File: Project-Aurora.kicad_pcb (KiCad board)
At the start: 4 copper layers, 285 x 94.6 mm, 266 parts, among them P1 USB_OTG, P2 FLASH_HDR, SW1 Reset, SW10 SW_PUSH, SW11 SW_PUSH, SW12 SW_PUSH, SW13 SW_PUSH, SW14 SW_PUSH, SW15 SW_PUSH, SW16 SW_PUSH, SW17 SW_PUSH, SW18 SW_PUSH, SW19 SW_PUSH, SW2 SW_PUSH, SW20 SW_PUSH, SW21 SW_PUSH, SW22 SW_PUSH, SW23 SW_PUSH, SW24 SW_PUSH, SW25 SW_PUSH, SW26 SW_PUSH, SW27 SW_PUSH, SW28 SW_PUSH, SW29 SW_PUSH, SW3 SW_PUSH, SW30 SW_PUSH, SW31 SW_PUSH, SW32 SW_PUSH, SW33 SW_PUSH, SW34 SW_PUSH, SW35 SW_PUSH, SW36 SW_PUSH, SW37 SW_PUSH, SW38 SW_PUSH, SW39 SW_PUSH, SW4 SW_PUSH, SW40 SW_PUSH, SW41 SW_PUSH, SW42 SW_PUSH, SW43 SW_PUSH, SW44 SW_PUSH, SW45 SW_PUSH, SW46 SW_PUSH, SW47 SW_PUSH, SW48 SW_PUSH, SW49 SW_PUSH, SW5 SW_PUSH, SW50 SW_PUSH, SW51 SW_PUSH, SW52 SW_PUSH, SW53 SW_PUSH, SW54 SW_PUSH, SW55 SW_PUSH, SW56 SW_PUSH, SW57 SW_PUSH, SW58 SW_PUSH, SW59 SW_PUSH, SW6 SW_PUSH, SW60 SW_PUSH, SW61 SW_PUSH, SW62 SW_PUSH, SW63 SW_PUSH, SW64 SW_PUSH, SW65 SW_PUSH, SW66 SW_PUSH, SW7 SW_PUSH, SW8 SW_PUSH, SW9 SW_PUSH, U1 IS31FL3732, U2 MK20DX256VLH7, U3 TPS62086, U4 IS31FL3732, U6 Case-Ground, X1 CRYSTAL_SMD

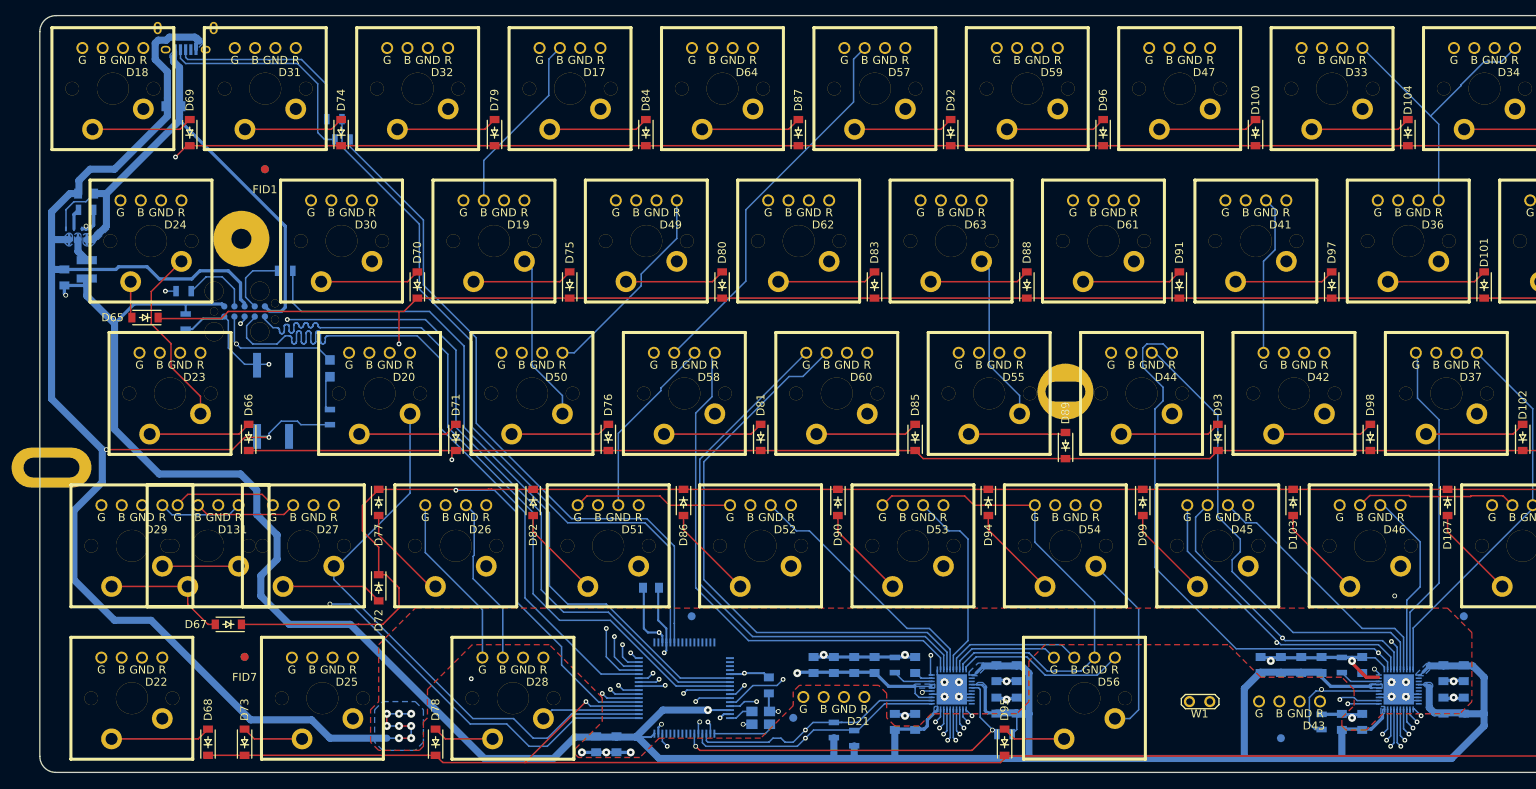
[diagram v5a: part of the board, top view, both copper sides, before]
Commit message: Switched from using a Dedicated one to the MCUs integrated Voltage Regulator for 3.3V. The LED-Drivers are now using 5V.
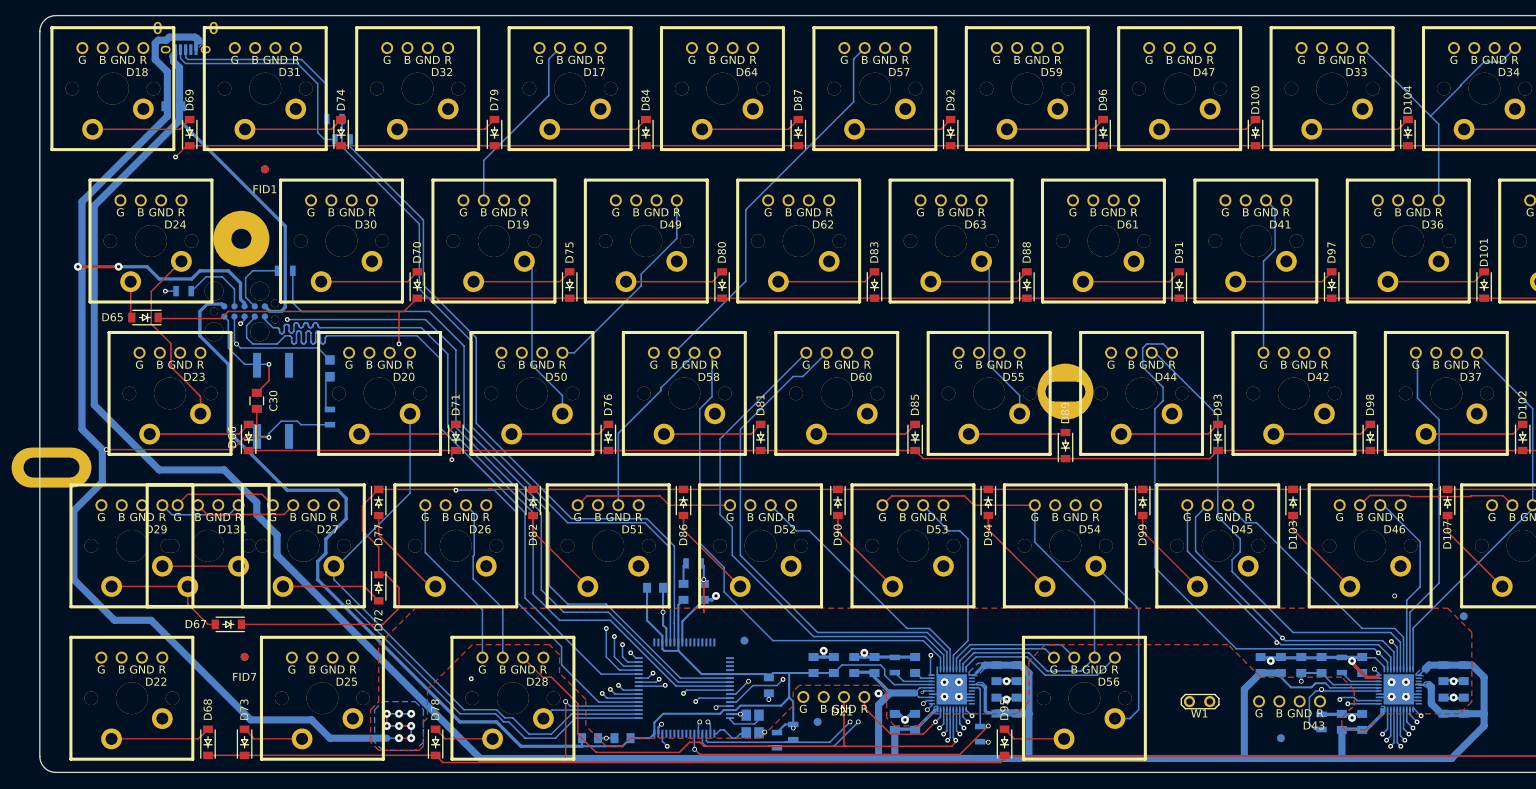
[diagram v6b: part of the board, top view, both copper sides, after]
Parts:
- removed L1: 470, Inductors_NEOSID:Neosid_Inductor_SM-NE29_SMD1008
- removed R3: 33, Resistors_SMD:R_0805
- removed the U3 at (67.1, 91.9)
- added C30: 100n, Capacitors_SMD:C_0805, F.Cu at (89.4, 112.8)
- C19, C21: value 22uF -> 2.2uF
- R7: value 1M -> 5M
- moved C21 91.9 mm to (145.3, 136.7), turned to 270 degrees
- moved R7 87.9 mm to (144.0, 133.1), turned to 0 degrees
- moved C19 86.8 mm to (142.7, 136.7)
- moved R10 9.66 mm to (154.4, 155.2), turned to 90 degrees
- moved FID9 7.27 mm to (150.4, 142.7)
- moved R8 5.09 mm to (156.5, 154.2), turned to 90 degrees
- moved FID10 3.09 mm to (159.5, 152.9)
- moved R4 3.05 mm to (179.8, 154.4), turned to 90 degrees
- moved X1 1.27 mm to (151.4, 153.2), turned to 270 degrees
- moved C15 1.08 mm to (131.1, 154.9), turned to 0 degrees
- moved C13 1.08 mm to (135.1, 154.9), turned to 180 degrees
- moved C1 0.51 mm to (139.2, 136.1)
- renumbered U2 to U1, U1 to U2, U4 to U3
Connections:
- net Net-(U2-Pad32) renamed /X+
- net Net-(U2-Pad33) renamed /X-
- C10 pad 1: +3V3 -> +5V
- C11 pad 1: +3V3 -> +5V
- C12 pad 1: +3V3 -> +5V
- C19 pad 1: GND -> Net-(C19-Pad1)
- C20 pad 2: /5V -> +5V
- C21 pad 2: /5V -> +5V
- C22 pad 1: +3V3 -> +5V
- C23 pad 1: +3V3 -> +5V
- C24 pad 1: +3V3 -> +5V
- C25 pad 1: +3V3 -> +5V
- C26 pad 1: +3V3 -> +5V
- C27 pad 1: +3V3 -> +5V
- C28 pad 1: +3V3 -> +5V
- C29 pad 1: +3V3 -> +5V
- C5 pad 1: +3V3 -> +5V
- C6 pad 1: +3V3 -> +5V
- C7 pad 1: +3V3 -> +5V
- C8 pad 1: +3V3 -> +5V
- C9 pad 1: +3V3 -> +5V
- P1 pad 1: /5V -> +5V
- P2 pad 5: /5V -> +5V
- R7 pad 1: +3V3 -> Net-(C19-Pad1)
- R7 pad 2: Net-(R7-Pad2) -> GND
- U1 pad 7: Net-(U2-Pad7) -> +3V3
- U1 pad 8: Net-(U2-Pad8) -> +5V
- U2 pad 1: +3V3 -> +5V
- U2 pad 20: +3V3 -> +5V
- U2 pad 26: +3V3 -> +5V
- U2 pad 4: +3V3 -> +5V
- U3 pad 1: +3V3 -> +5V
- U3 pad 20: +3V3 -> +5V
- U3 pad 23: +3V3 -> +5V
- U3 pad 26: +3V3 -> +5V
- U3 pad 4: +3V3 -> +5V
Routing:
- net +5V: track 0.00 -> 439.3 mm, vias 0 -> 2
- net +3V3: track 457.7 -> 269.6 mm, vias 6 -> 3
- net /5V: track 70.8 -> 0.00 mm
- net GND: track 323.9 -> 307.8 mm, vias 36 -> 37
- net /SDA: track 111.8 -> 98.3 mm, vias 2 -> 3
- net /SCL: track 112.2 -> 99.7 mm, vias 2 -> 3
- net /LED2A/CA3: track 232.1 -> 223.6 mm
- net /LED2A/CA2: track 229.0 -> 222.4 mm
- net /MCU_RESET: track 108.9 -> 104.9 mm
- net /Keymatrix/Col13: track 261.5 -> 264.6 mm
- net Net-(L1-Pad1): track 3.02 -> 0.00 mm
- net /X-: track 7.76 -> 4.87 mm
- net Net-(C19-Pad1): track 0.00 -> 2.69 mm
- net /LED2B/CB5: track 70.3 -> 72.9 mm
- net Net-(R7-Pad2): track 2.61 -> 0.00 mm
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- added copper zone on B.Cu, net +5V
- removed copper zone on B.Cu, net +3V3
- removed copper zone on B.Cu, net /5V
- removed copper zone on B.Cu, net Net-(L1-Pad1)

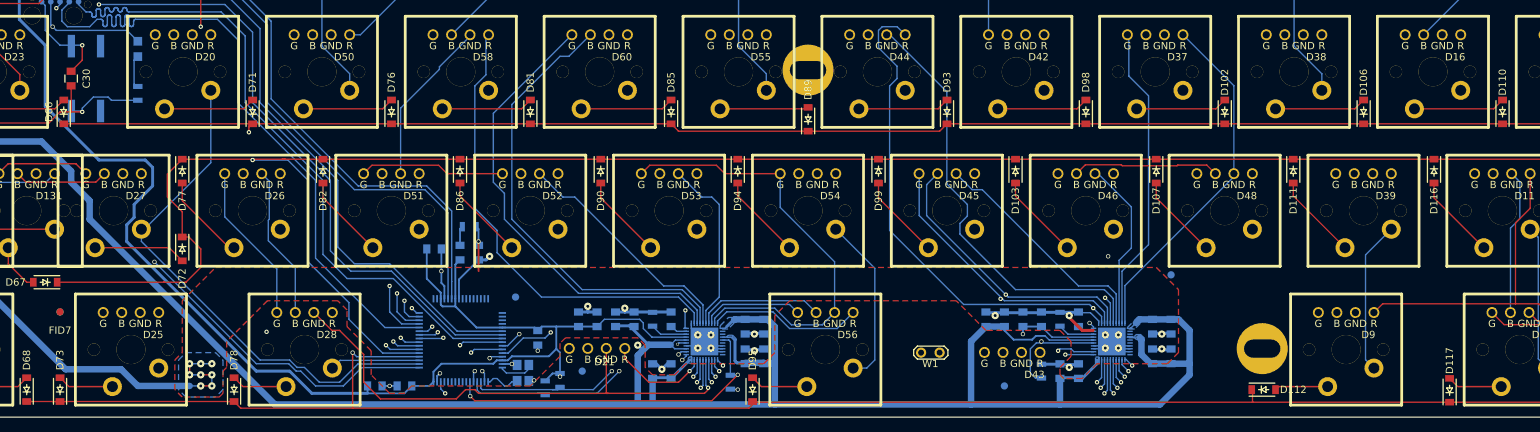
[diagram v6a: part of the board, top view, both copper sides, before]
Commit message: Cleaned up some Routing Stuff.
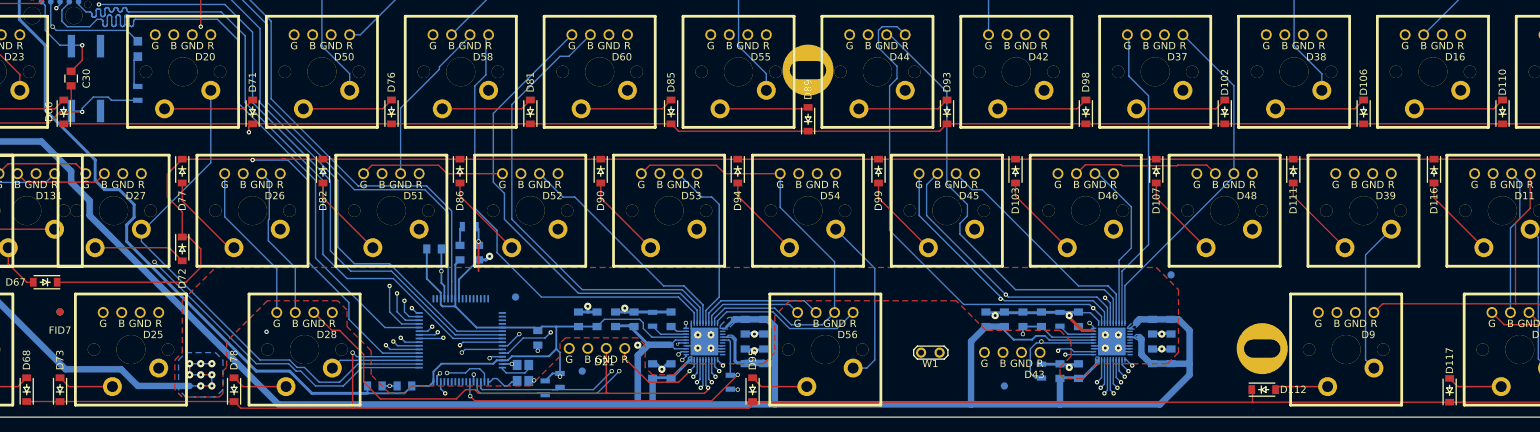
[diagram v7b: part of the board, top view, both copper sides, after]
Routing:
- net /Keymatrix/Col12: track 256.0 -> 244.1 mm
- net +3V3: track 269.6 -> 265.0 mm
- net /Keymatrix/Col11: track 218.8 -> 222.2 mm
- net /Keymatrix/Col10: track 188.7 -> 192.1 mm
- net /LED1A/CA4: track 130.1 -> 133.2 mm, vias 2 -> 1
- net /LED2B/CB6: track 191.8 -> 189.1 mm
- net /Sync: track 60.0 -> 57.5 mm
- net /LED1A/CA1: track 220.6 -> 222.8 mm
- net /LED1B/CB2: track 266.7 -> 266.0 mm

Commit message: Properly named Case Ground.
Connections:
- net GNDPWR renamed GNDCase
